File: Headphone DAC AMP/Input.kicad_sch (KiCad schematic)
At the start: 17 parts, among them J1 USB_C_Receptacle, U2 XU316-1024-QF60B-C24, U8 W25Q16JVSNIQ, U9 NUP2202

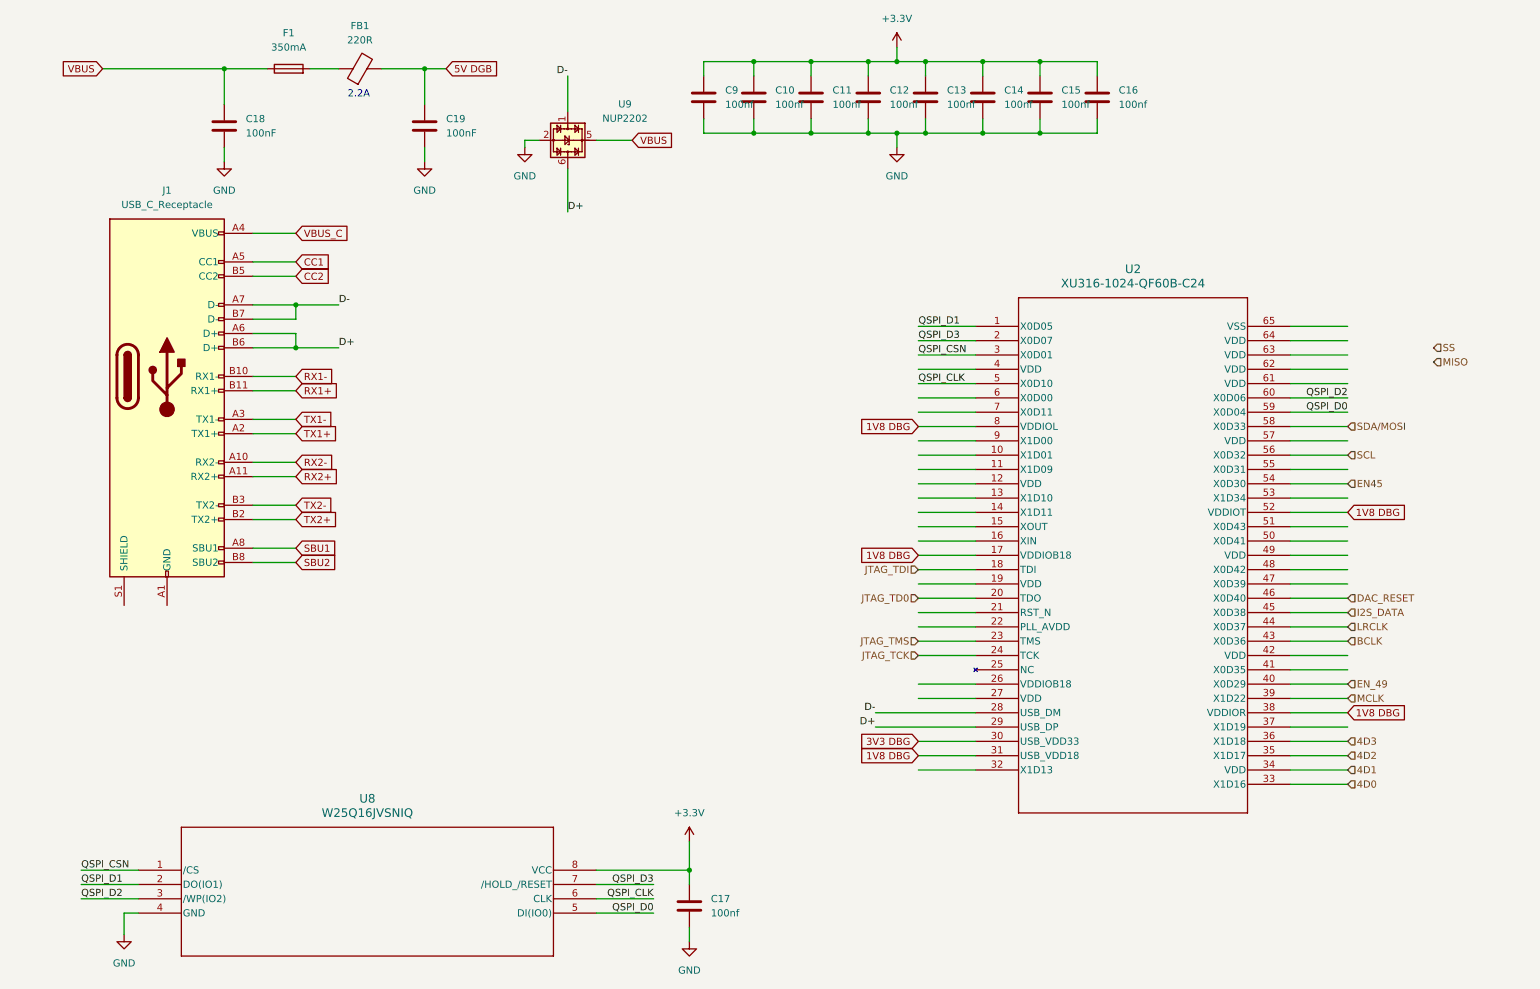
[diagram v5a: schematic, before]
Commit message: Completed a significant amount of the power and routing
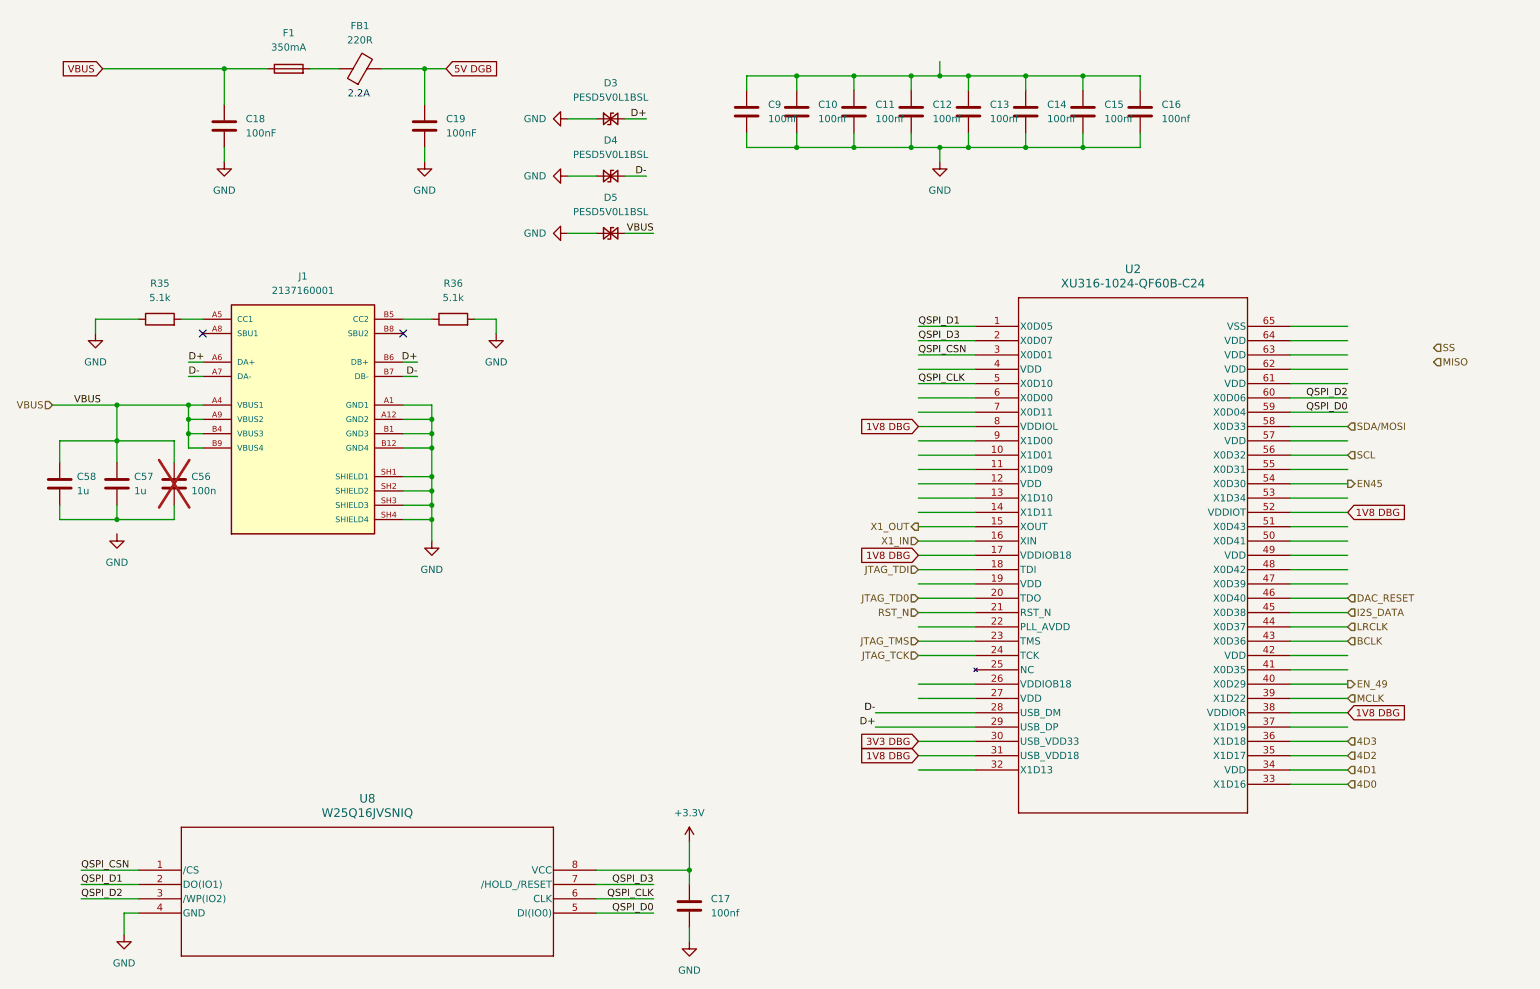
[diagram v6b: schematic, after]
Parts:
- removed J1: USB_C_Receptacle, symbol Connector:USB_C_Receptacle
- removed U9: NUP2202, Package_TO_SOT_SMD:SOT-363_SC-70-6, symbol Power_Protection:NUP2202
- added C56: 100n, Capacitor_SMD:C_0805_2012Metric_Pad1.18x1.45mm_HandSolder, symbol Device:C
- added C57, C58: 1u, Capacitor_SMD:C_0805_2012Metric_Pad1.18x1.45mm_HandSolder, symbol Device:C
- added D3, D4, D5: PESD5V0L1BSL, Diode_SMD:D_SOD-882, symbol Device:D_TVS_Small
- added J1: 2137160001, 2137160001:MOLEX_2137160001, symbol 2137160001:2137160001
- added R35, R36: 5.1k, Resistor_SMD:R_0805_2012Metric_Pad1.20x1.40mm_HandSolder, symbol Device:R
- C10, C11, C12, C13, C14, C15, C16, C17, C18, C19, C9: footprint (none) -> Capacitor_SMD:C_0805_2012Metric_Pad1.18x1.45mm_HandSolder
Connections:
- net +3.3V: no longer C10.1, C11.1, C12.1, C13.1, C14.1, C15.1, C16.1, C9.1
- net D+: now also D3.2 (A2), J1.A6 (DA+), J1.B6 (DB+)
- net D-: now also D4.2 (A2), J1.A7 (DA-), J1.B7 (DB-)
- net GND: now also D3.1 (A1), D4.1 (A1), D5.1 (A1), J1.A1 (GND1), J1.A12 (GND2), J1.B1 (GND3), J1.B12 (GND4), J1.SH1 (SHIELD1), J1.SH2 (SHIELD2), J1.SH3 (SHIELD3), J1.SH4 (SHIELD4), R35.1, R36.2
- net VBUS: now also C56.1, C57.1, C58.1, D5.2 (A2), J1.A4 (VBUS1), J1.A9 (VBUS2), J1.B4 (VBUS3), J1.B9 (VBUS4)
- net X1_OUT: now reaches U2.15 (XOUT)
- net X1_IN: now reaches U2.16 (XIN)
- net RST_N: now reaches U2.21 (RST_N)
- new net: J1.B5 (CC2), R36.1
- new net: C10.1, C11.1, C12.1, C13.1, C14.1, C15.1, C16.1, C9.1
- new net: C56.2, C57.2, C58.2
- new net: J1.A5 (CC1), R35.2
- no-connect marks 0 -> 2
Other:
- moved on the sheet: C10, C11, C12, C13, C14, C15, C16, C9

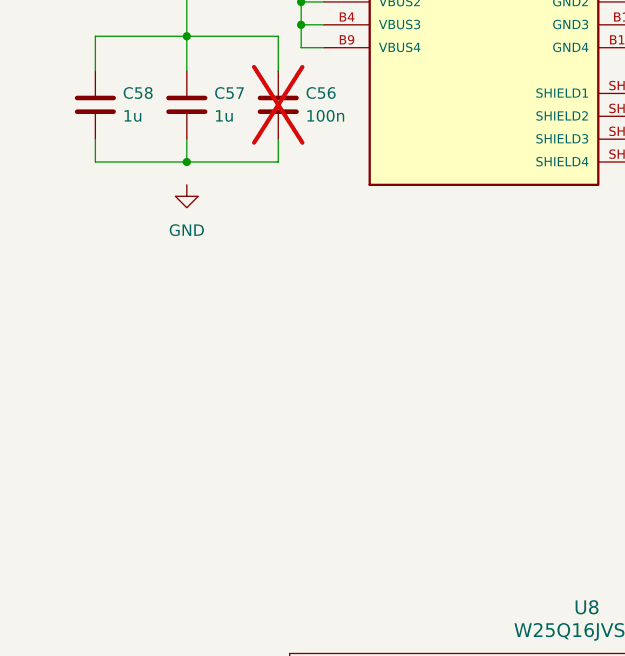
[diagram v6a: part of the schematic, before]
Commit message: Added ground and 0.9v
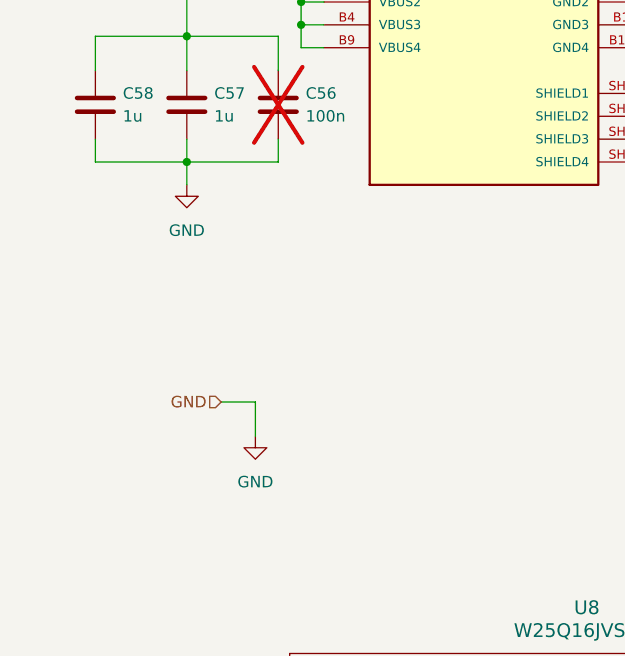
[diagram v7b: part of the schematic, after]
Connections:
- net GND: now also C56.2, C57.2, C58.2
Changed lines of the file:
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@@
+	(wire
+		(pts
+			(xy 34.29 101.6) (xy 34.29 104.14)
+		)
+		(stroke
+			(width 0)
+			(type default)
+		)
+	)
 	(wire
 		(pts
@@
 	(wire
 		(pts
+			(xy 41.91 128.27) (xy 41.91 132.08)
+		)
+		(stroke
+			(width 0)
+			(type default)
+		)
+	)
+	(wire
+		(pts
 			(xy 154.94 22.86) (xy 154.94 25.4)
 		)
@@
 		(pts
 			(xy 242.57 74.93) (xy 252.73 74.93)
+		)
+		(stroke
+			(width 0)
+			(type default)
+		)
+	)
+	(wire
+		(pts
+			(xy 38.1 128.27) (xy 41.91 128.27)
 		)
 		(stroke
@@
 		(shape input)
 		(at 22.86 81.28 180)
+		(effects
+			(font
+				(size 1.27 1.27)
+			)
+			(justify right)
+		)
+	)
+	(hierarchical_label "GND"
+		(shape input)
+		(at 38.1 128.27 180)
 		(effects
 			(font
@@
 					(unit 1)
 				)
+			)
+		)
+	)
+	(symbol
+		(lib_id "power:GND")
+		(at 41.91 132.08 0)
+		(unit 1)
+		(exclude_from_sim no)
+		(in_bom yes)
+		(on_board yes)
+		(dnp no)
+		(fields_autoplaced yes)
+		(property "Reference" "#PWR081"
+			(at 41.91 138.43 0)
+			(effects
+				(font
+					(size 1.27 1.27)
+				)
+				(hide yes)
+			)
+		)
+		(property "Value" "GND"
+			(at 41.91 137.16 0)
+			(effects
+				(font
+					(size 1.27 1.27)
+				)
+			)
+		)
+		(property "Footprint" ""
+			(at 41.91 132.08 0)
+			(effects
+				(font
+					(size 1.27 1.27)
+				)
+				(hide yes)
+			)
+		)
+		(property "Datasheet" ""
+			(at 41.91 132.08 0)
+			(effects
+				(font
+					(size 1.27 1.27)
+				)
+				(hide yes)
+			)
+		)
+		(property "Description" "Power symbol creates a global label with name \"GND\" , ground"
+			(at 41.91 132.08 0)
+			(effects
+				(font
+					(size 1.27 1.27)
+				)
+				(hide yes)
+			)
+		)
+		(pin "1"
+		)
+		(instances
+			(project "Headphone DAC AMP"
+				(path "/d034eddd-efbc-47be-a25c-37cbfbab4cd8/2765e1cc-205a-4739-b769-20b95f3d1fdb"
+					(reference "#PWR081")
+					(unit 1)
+				)

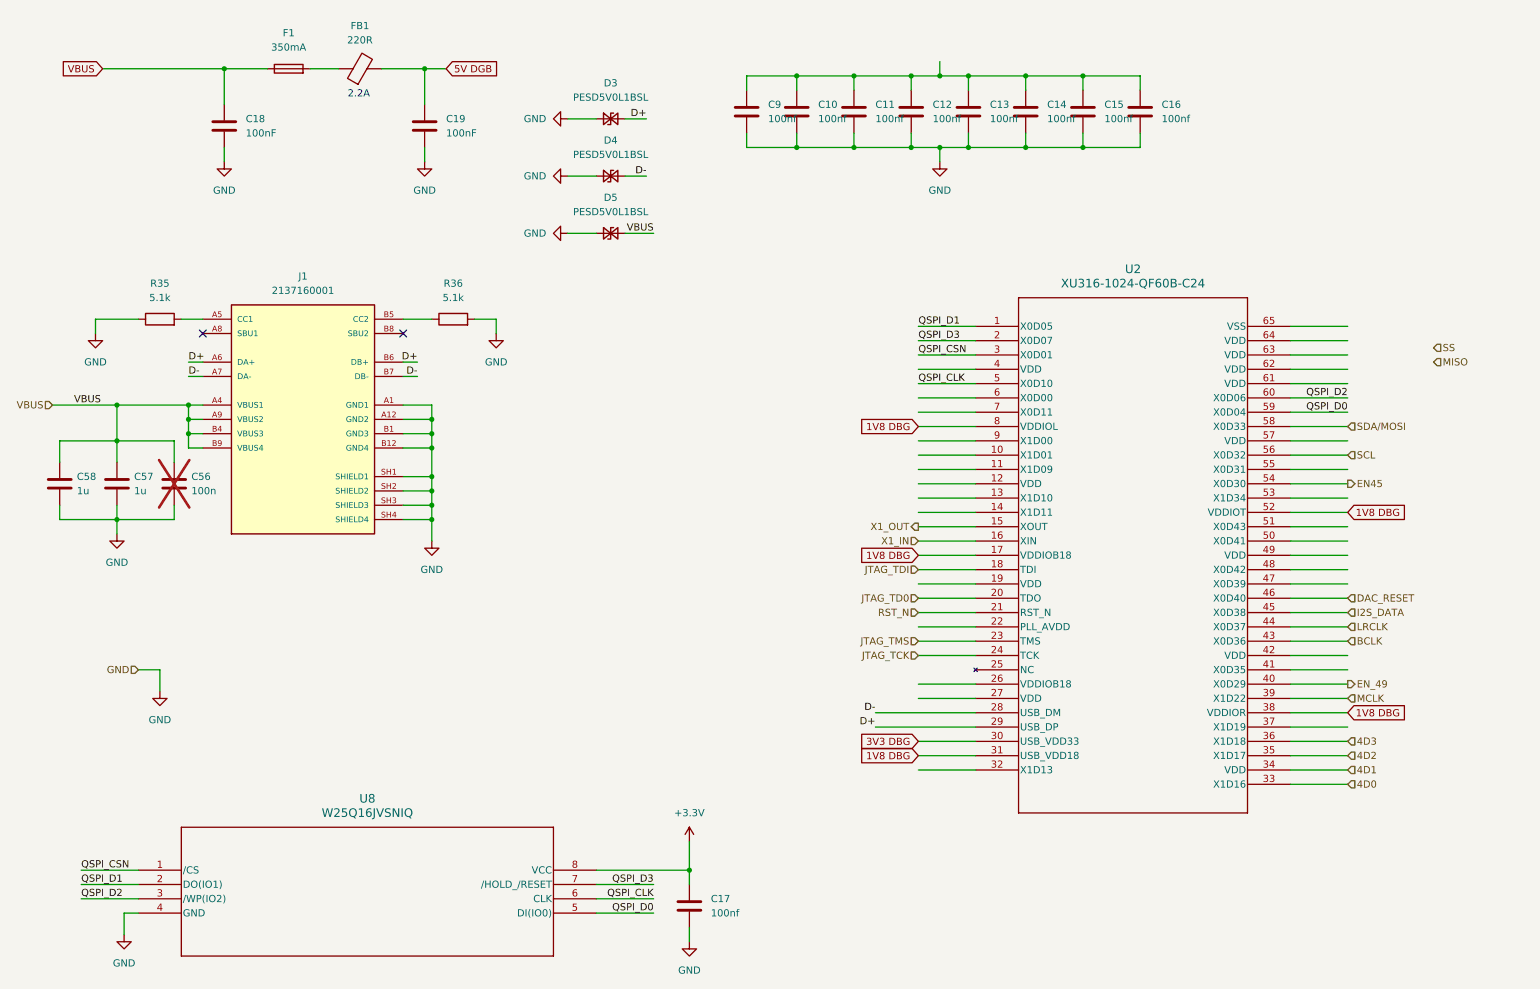
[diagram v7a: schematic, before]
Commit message: Polished DAC GPIOs and connected to XMOS
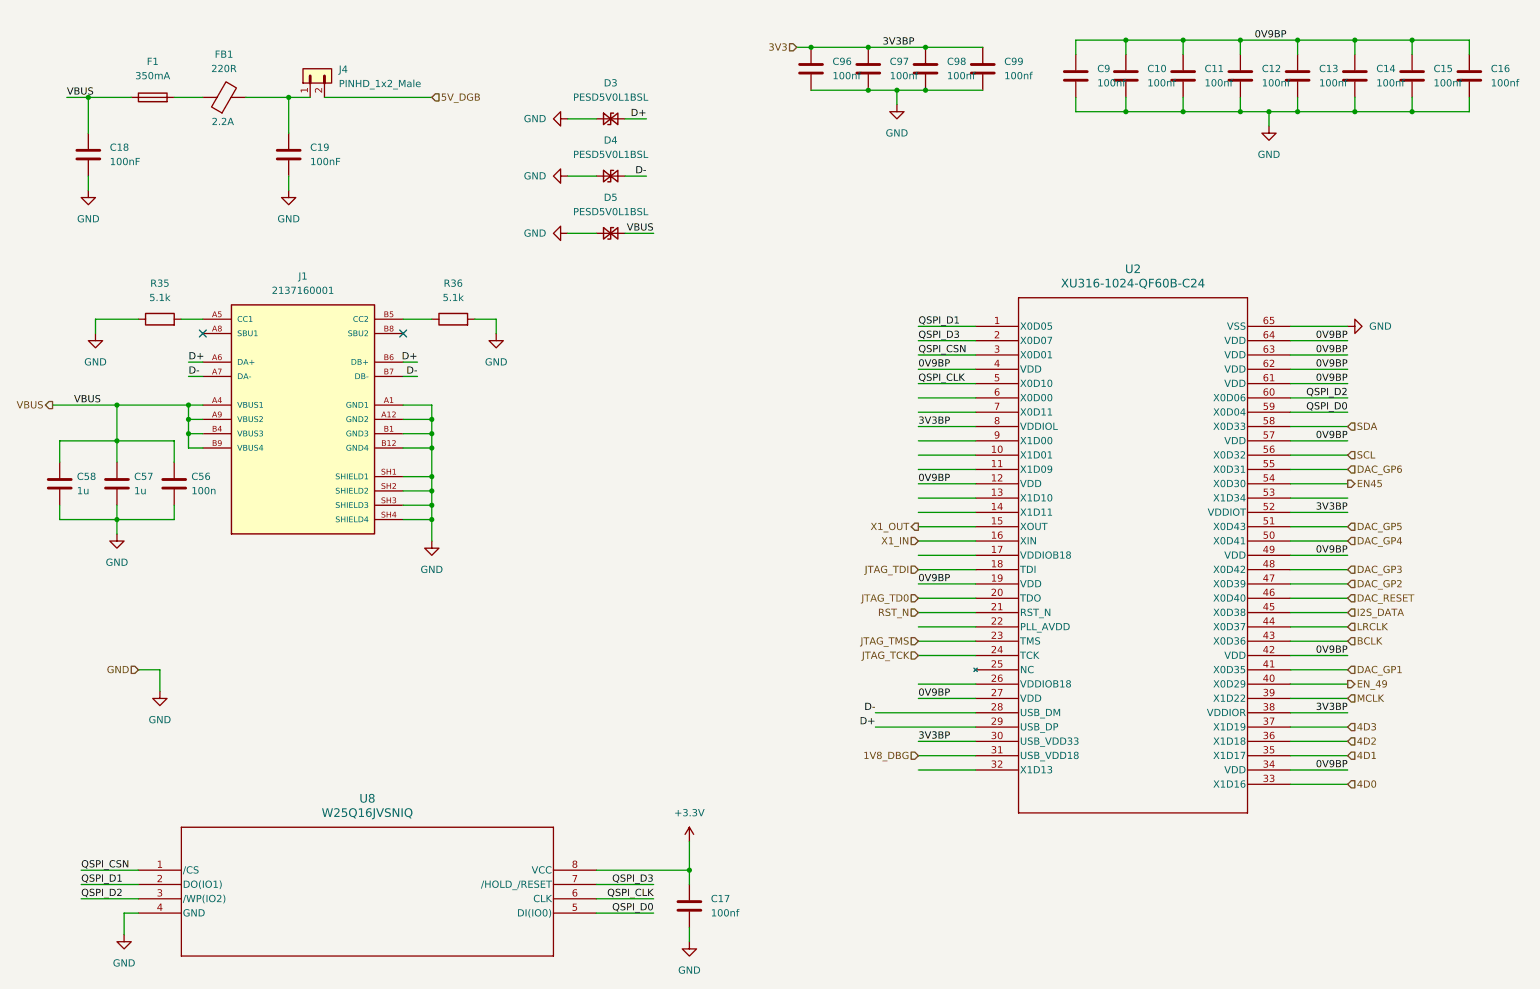
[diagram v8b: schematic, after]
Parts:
- added C96, C97, C98, C99: 100nf, Capacitor_SMD:C_0805_2012Metric_Pad1.18x1.45mm_HandSolder, symbol Device:C
- added J4: PINHD_1x2_Male, Connector_PinHeader_2.54mm:PinHeader_1x02_P2.54mm_Vertical, symbol PCM_SL_Pin_Headers:PINHD_1x2_Male
- C56: now fitted
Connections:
- net 3V3 DBG is gone; now on net 3V3: U2.30 (USB_VDD33)
- net 4D1: now also U2.35 (X1D17); no longer U2.34 (VDD)
- net 4D2: now also U2.36 (X1D18); no longer U2.35 (X1D17)
- net 4D3: now also U2.37 (X1D19); no longer U2.36 (X1D18)
- net GND: now also U2.65 (VSS), C96.2, C97.2, C98.2, C99.2
- net 0V9BP: now reaches C10.1, C11.1, C12.1, C13.1, C14.1, C15.1, C16.1, C9.1
- net 0V9BP: now also U2.12 (VDD), U2.19 (VDD), U2.27 (VDD), U2.34 (VDD), U2.4 (VDD), U2.42 (VDD), U2.49 (VDD), U2.57 (VDD), U2.61 (VDD), U2.62 (VDD), U2.63 (VDD), U2.64 (VDD)
- net DAC_GP1: now reaches U2.41 (X0D35)
- net DAC_GP2: now reaches U2.47 (X0D39)
- net DAC_GP3: now reaches U2.48 (X0D42)
- net DAC_GP4: now reaches U2.50 (X0D41)
- net DAC_GP5: now reaches U2.51 (X0D43)
- net DAC_GP6: now reaches U2.55 (X0D31)
- net 1V8 DBG renamed 3V3
- net 3V3: now also C96.1, C97.1, C98.1, C99.1; no longer U2.17 (VDDIOB18), U2.31 (USB_VDD18)
- net 5V DGB: no longer names the net of C19.1, FB1.2
- net 5V DGB: now also J4.1
- net SDA/MOSI renamed SDA
- new net 1V8_DBG: U2.31 (USB_VDD18)
- new net 5V_DGB: J4.2
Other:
- moved on the sheet: C10, C11, C12, C13, C14, C15, C16, C18, C19, C9, F1, FB1
